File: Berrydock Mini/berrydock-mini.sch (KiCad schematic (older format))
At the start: 96 parts, among them J1 RJ45, P1 CONN_01X18, P2 CONN_01X18, P3 CONN_01X04, P4 CONN_01X02, P5 USB_OTG, P6 USB_A, SW1 SWITCH_INV, SW2 BUTTON, U1 USBLC6-2, U10 L6920DC, U11 FS8205A, U12 DW01-P, U13 USBLC6-2, U14 ADS1015, U15 USBLC6-2, U16 CP2102, U2 USBLC6-2, U3 AMS1117, U4 H1260NL, U5 Omega2, U6 SMP75, U7 SMP75, U8 ACT4088, U9 MCP73831

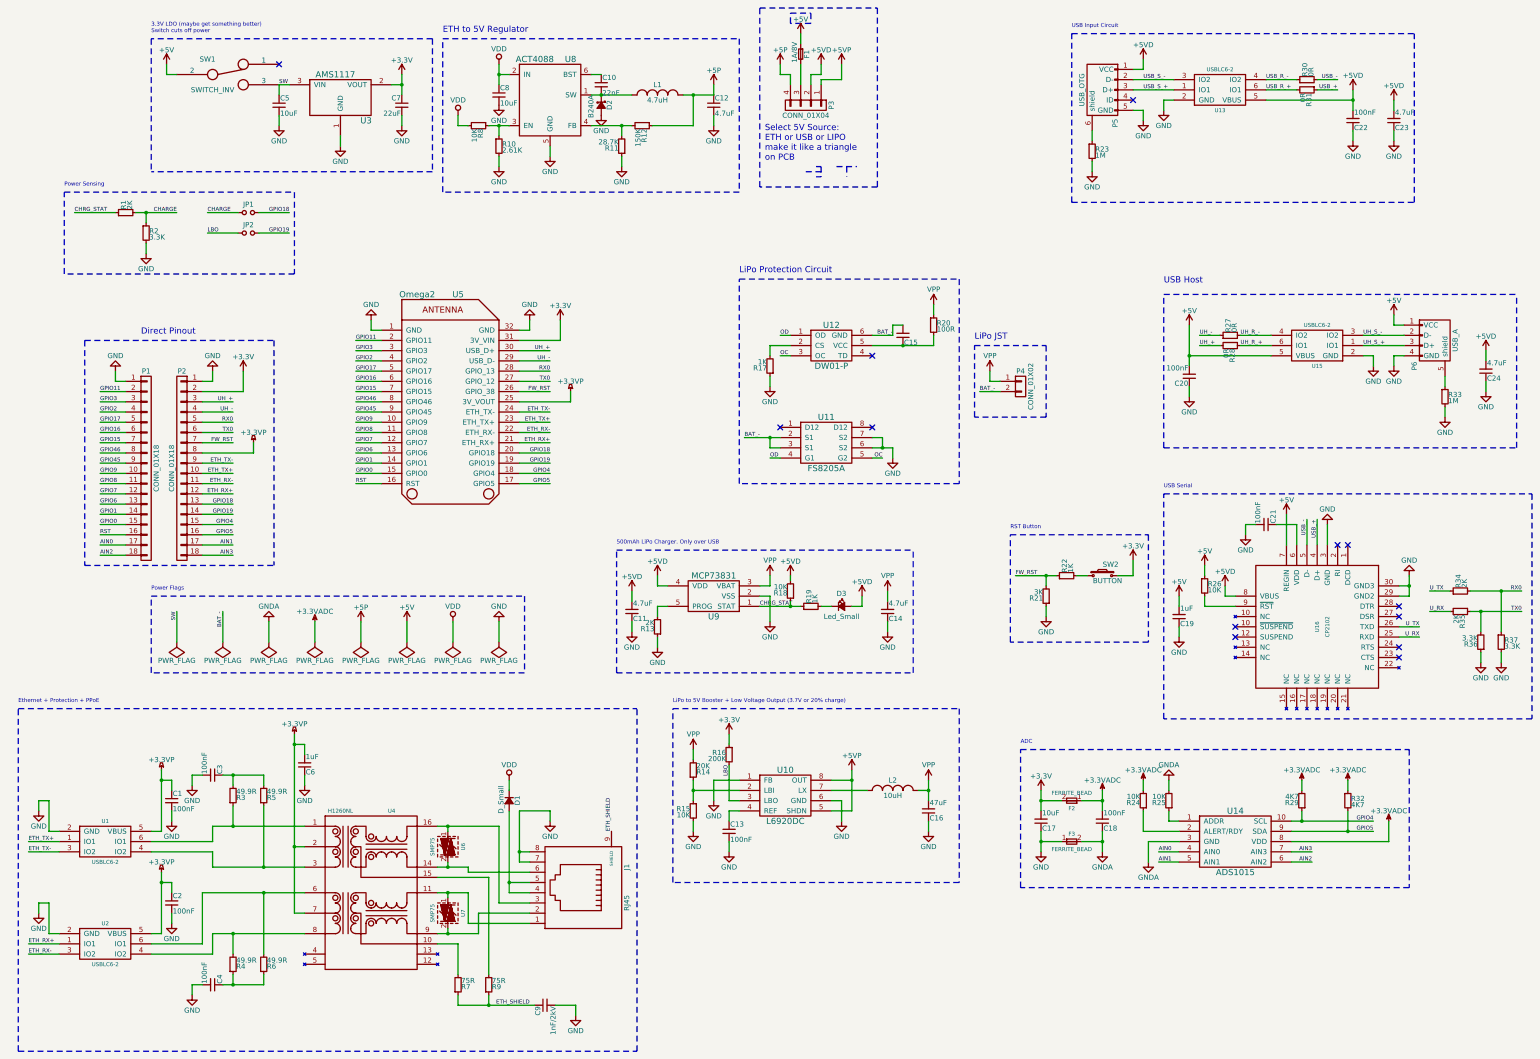
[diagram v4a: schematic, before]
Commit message: Added many footprint
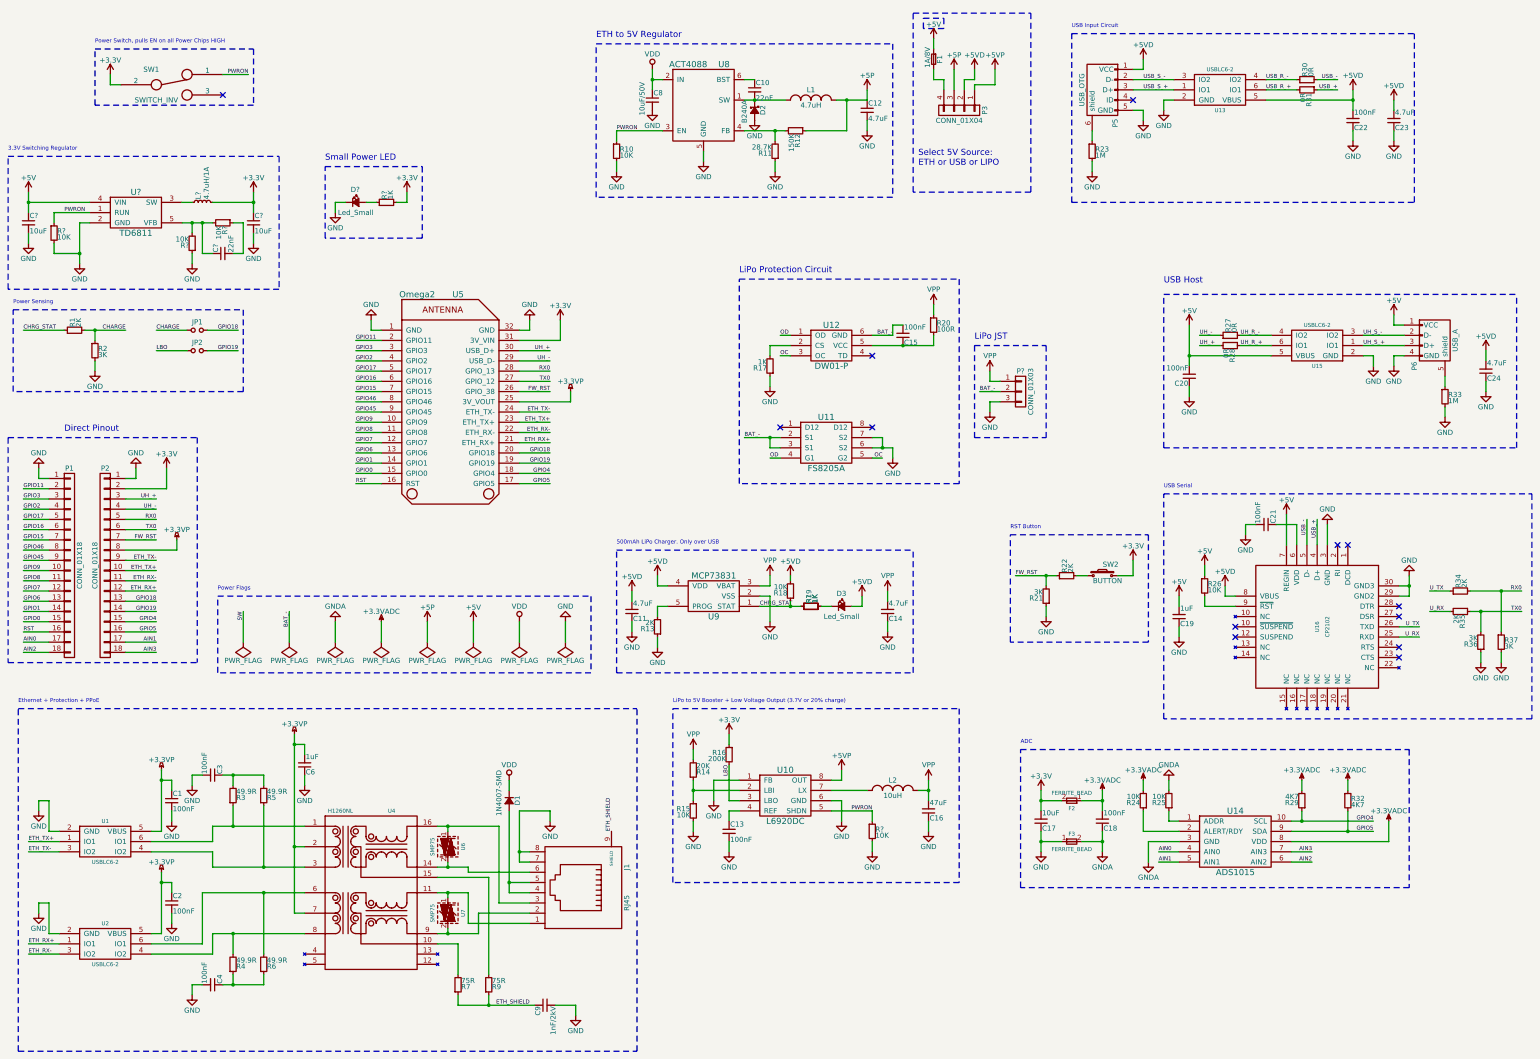
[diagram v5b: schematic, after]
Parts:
- removed C5: 10uF, Capacitors_SMD:C_0603, symbol C_Small
- removed C7: 22uF, Capacitors_SMD:C_0603, symbol C_Small
- removed P4: CONN_01X02, symbol CONN_01X02
- removed R8: 10K, Resistors_SMD:R_0603_HandSoldering, symbol R_Small
- removed U3: AMS1117, symbol AMS1117
- added C? (x2): 10uF, Capacitors_SMD:C_1206, symbol C_Small
- added C?: 22nF, Capacitors_SMD:C_1206, symbol C_Small
- added D?: Led_Small, LEDs:LED_0805, symbol Led_Small
- added L?: 4.7uH/1A, symbol L_Small
- added P?: CONN_01X03, Omega2-Berrydock:JST-RIGHT-ANGLE, symbol CONN_01X03
- added R? (x2): 1K, Resistors_SMD:R_0603_HandSoldering, symbol R_Small
- added R? (x4): 10K, Resistors_SMD:R_0603_HandSoldering, symbol R_Small
- added U?: TD6811, symbol TD6811
- C1, C11: footprint (none) -> Capacitors_SMD:C_0603
- C15: value Capacitors_SMD:C_0603 -> 100nF; footprint (none) -> Capacitors_SMD:C_0603
- C8: value 10uF -> 10uF/50V
- D1: value D_Small -> 1N4007-SMD; footprint (none) -> Omega2-Berrydock:DO-214AC.SMA
- D2: footprint (none) -> Omega2-Berrydock:DO-214AC.SMA
- D3: footprint (none) -> LEDs:LED_0805
- J1: footprint (none) -> Omega2-Berrydock:RJ45-SHIELDED
- JP1, JP2: footprint (none) -> Pin_Headers:Pin_Header_Straight_1x02
- L1: footprint (none) -> Omega2-Berrydock:CD32
- P3: footprint (none) -> Omega2-Berrydock:PWR-SELECT
- P5: footprint (none) -> Connect:USB_Micro-B
- P6: footprint (none) -> Connect:USB_A
- R10: value 2.61K -> 10K
- R2, R36, R37: value 3.3K -> 3K
- R22: value 1K -> 2K
- U1, U13, U15, U2: footprint (none) -> Omega2-Berrydock:SOT32-6L
- U11: footprint (none) -> Omega2-Berrydock:TSSOP8
- U12, U8: footprint (none) -> TO_SOT_Packages_SMD:SOT-23-6_Handsoldering
- U16: footprint (none) -> Housings_DFN_QFN:QFN-28-1EP_5x5mm_Pitch0.5mm
- U4: footprint (none) -> Omega2-Berrydock:HL1260NL
- U5: footprint (none) -> Omega2-Berrydock:Omega2-Outline
- U6, U7: footprint (none) -> Omega2-Berrydock:DO-214AA
- U9: footprint (none) -> TO_SOT_Packages_SMD:SOT-23-5
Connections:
- net +3V3: now also SW1.2, C?.1, L?.2, R?.2
- net +5P: now also P3.3 (P3); no longer P3.4 (P4)
- net +5V: now also C?.1, U?.4 (VIN); no longer SW1.2
- net +5VP: no longer U10.5 (SHDN)
- net BAT_-: now also P?.2 (P2)
- net CHRG_STAT: now also R?.1
- net GND: now also C?.2, C?.2, D?.1 (K), P?.3 (P3), R?.1, R?.2, R?.2, U?.2 (GND)
- net SW: no longer SW1.3
- net VPP: now also P?.1 (P1)
- net PWRON: now reaches R10.1, U8.3 (EN)
- net PWRON: now also SW1.1, U10.5 (SHDN), R?.1, R?.1, U?.1 (RUN)
- net at F1.2: now also P3.4 (P4); no longer P3.3 (P3)
- net at D3.1 (K), R19.2: now also R?.2
- new net: L?.1, U?.3 (SW)
- new net: C?.1, R?.2, R?.2, U?.5 (VFB)
- new net: C?.2, R?.1
- new net: D?.2 (A), R?.1
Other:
- note added: "3.3V Switching Regulator"
- note added: "Power Switch, pulls EN on all Power Chips HIGH"
- note added: "Select 5V Source:\nETH or USB or LIPO\n"
- note added: "Small Power LED"
- note removed: "3.3V LDO (maybe get something better)\nSwitch cuts off power"
- note removed: "Select 5V Source:\nETH or USB or LIPO\nmake it like a triangle\non PCB"
- moved on the sheet: C10, C12, C8, D2, F1, JP1, JP2, L1, P1, P2, P3, R1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

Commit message: fixed errors, new naming of items
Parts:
- gave numbers to parts that had none: 13
- renumbered C8 to C10, C13 to C12, C10 to C13, C12 to C14, C14 to C17, C17 to C18, C18 to C19, C1 to C2, C19 to C20, C20 to C21, C21 to C22, C22 to C23, C23 to C24, C24 to C25, C2 to C3, C3 to C4, C4 to C5, C6 to C8, D1 to D2, D2 to D3, D3 to D4, L1 to L2, L2 to L3, R7 to R11, R9 to R12, R10 to R13, R13 to R16, R16 to R17, R17 to R18, R11 to R19, R1 to R2, R12 to R20, R18 to R21, R19 to R22, R20 to R25, R21 to R26, R22 to R27, R23 to R28, R24 to R29, R2 to R3, R25 to R30, R26 to R31, R27 to R32, R28 to R33, R29 to R34, R30 to R35, R31 to R36, R32 to R37, R33 to R38, R34 to R39, R35 to R40, R36 to R41, R37 to R42, R3 to R6, R4 to R7, R5 to R8, R6 to R9
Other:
- moved on the sheet: C11, C17, D4, R16, R21, R22, R23, U9

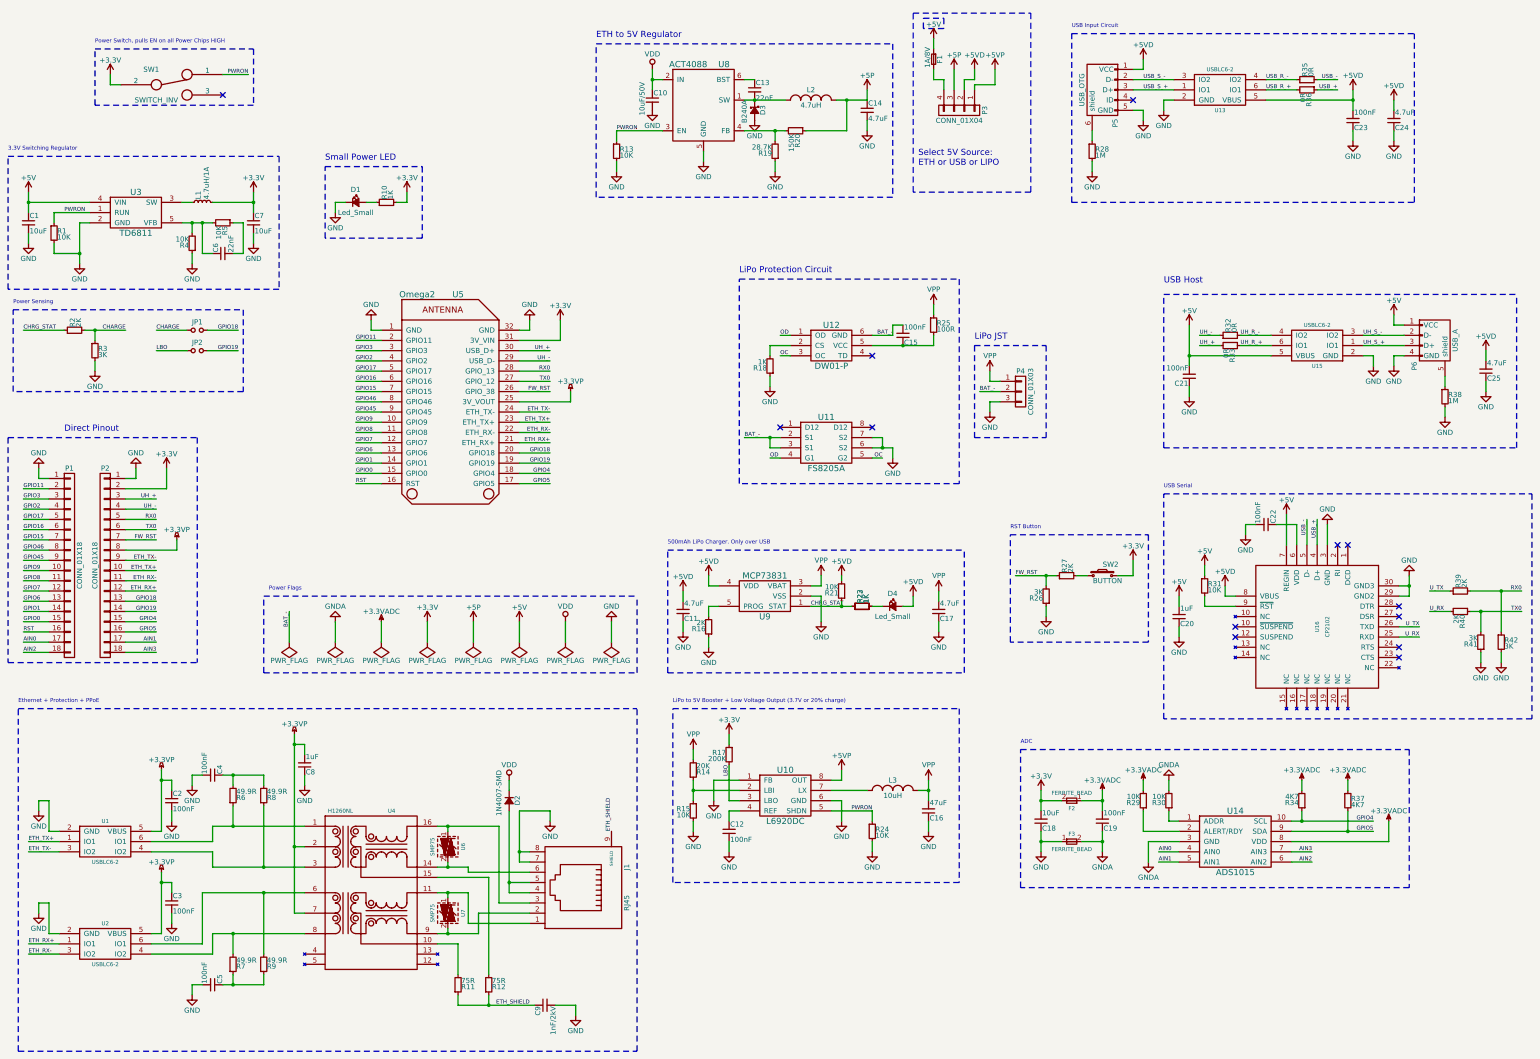
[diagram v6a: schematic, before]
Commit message: Added all footprints
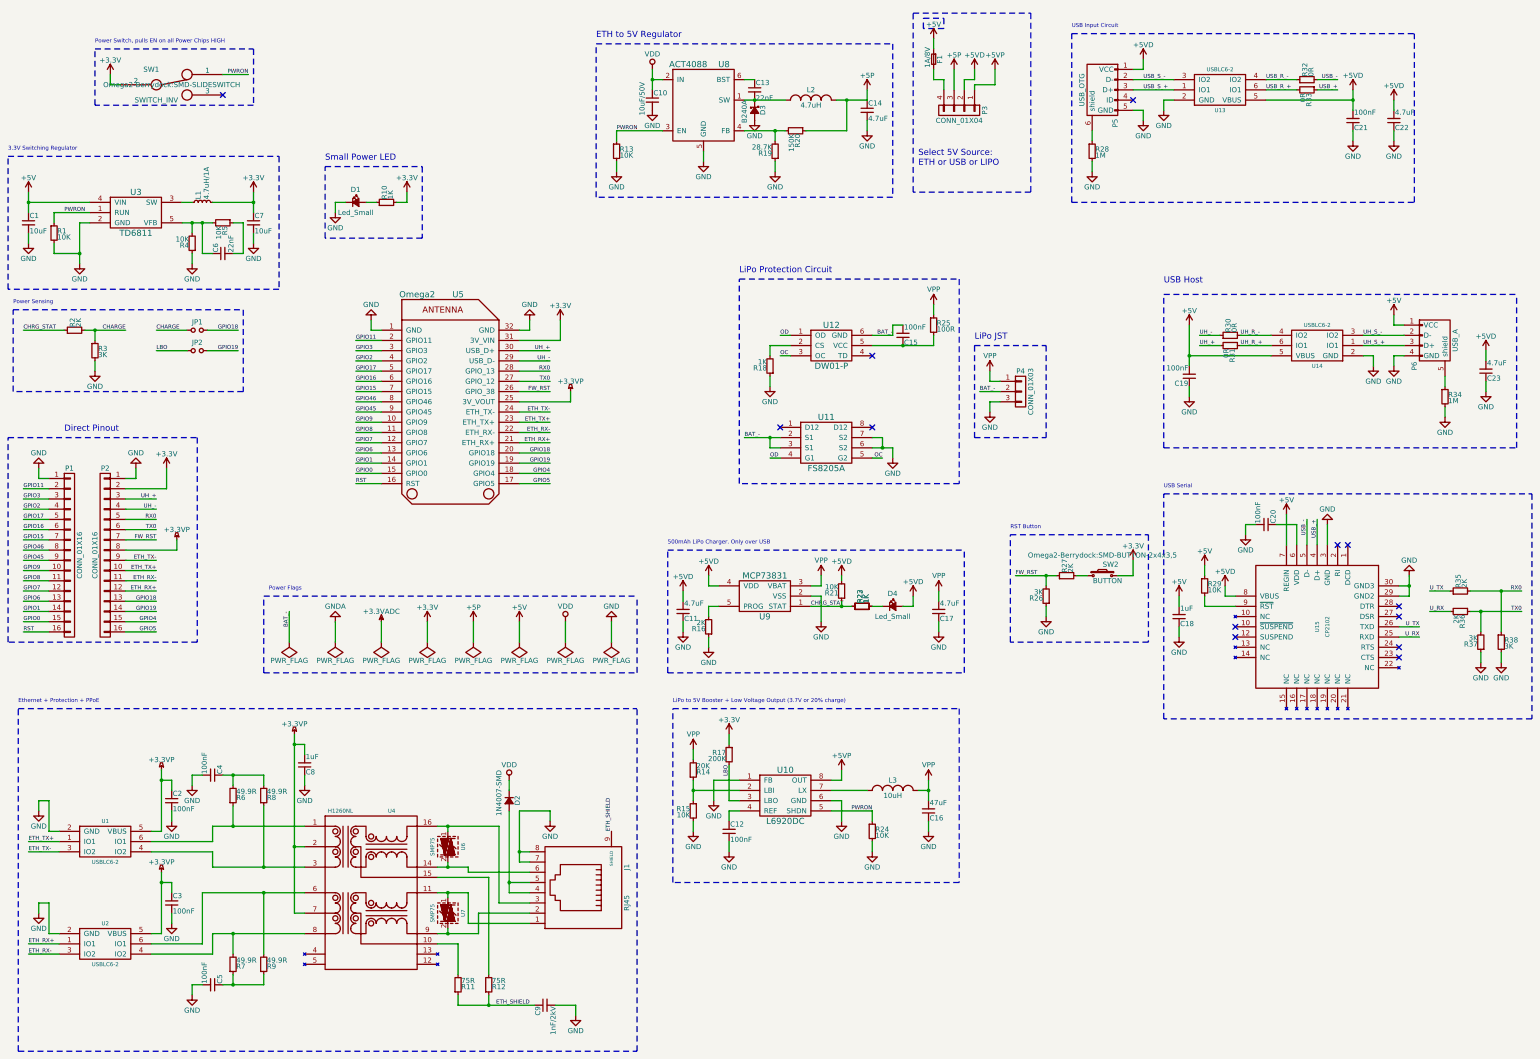
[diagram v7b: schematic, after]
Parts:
- removed C18: 10uF, Capacitors_SMD:C_0603, symbol C_Small
- removed C19: 100nF, Capacitors_SMD:C_0603, symbol C_Small
- removed F2, F3: FERRITE_BEAD, symbol FERRITE_BEAD
- removed P1, P2: CONN_01X18, Pin_Headers:Pin_Header_Straight_1x18, symbol CONN_01X18
- removed R29, R30: 10K, Resistors_SMD:R_0603_HandSoldering, symbol R_Small
- removed R34, R37: 4K7, Resistors_SMD:R_0603_HandSoldering, symbol R_Small
- removed U14: ADS1015, symbol ADS1015
- added P1, P2: CONN_01X16, Pin_Headers:Pin_Header_Straight_1x16, symbol CONN_01X16
- C19: renamed from C21; footprint (none) -> Capacitors_SMD:C_0603
- C8: footprint (none) -> Capacitors_SMD:C_0603
- F1: footprint (none) -> Omega2-Berrydock:FUSE-1812
- L1: footprint (none) -> Omega2-Berrydock:CD32
- L3: footprint (none) -> Omega2-Berrydock:CD43
- SW1: footprint (none) -> Omega2-Berrydock:SMD-SLIDESWITCH
- SW2: footprint (none) -> Omega2-Berrydock:SMD-BUTTON-2x4x3,5
- U10: footprint (none) -> Omega2-Berrydock:MSOP8
- U3: footprint (none) -> TO_SOT_Packages_SMD:SOT-23-5
- renumbered C20 to C18, C22 to C20, C23 to C21, C24 to C22, C25 to C23, R31 to R29, R32 to R30, R33 to R31, R35 to R32, R36 to R33, R38 to R34, R39 to R35, R40 to R36, R41 to R37, R42 to R38, U15 to U14, U16 to U15
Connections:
- net +3.3VP: now also P2.8 (P8)
- net +3V3: now also P2.2 (P2)
- net ETH_RX+: now also P2.12 (P12)
- net ETH_RX-: now also P2.11 (P11)
- net ETH_TX+: now also P2.10 (P10)
- net ETH_TX-: now also P2.9 (P9)
- net FW_RST: now also P2.7 (P7)
- net GND: now also P1.1 (P1), P2.1 (P1)
- net GPIO0: now also P1.15 (P15)
- net GPIO1: now also P1.14 (P14)
- net GPIO11: now also P1.2 (P2)
- net GPIO15: now also P1.7 (P7)
- net GPIO16: now also P1.6 (P6)
- net GPIO17: now also P1.5 (P5)
- net GPIO18: now also P2.13 (P13)
- net GPIO19: now also P2.14 (P14)
- net GPIO2: now also P1.4 (P4)
- net GPIO3: now also P1.3 (P3)
- net GPIO4: now also P2.15 (P15)
- net GPIO45: now also P1.9 (P9)
- net GPIO46: now also P1.8 (P8)
- net GPIO5: now also P2.16 (P16)
- net GPIO6: now also P1.13 (P13)
- net GPIO7: now also P1.12 (P12)
- net GPIO8: now also P1.11 (P11)
- net GPIO9: now also P1.10 (P10)
- net RST: now also P1.16 (P16)
- net RX0: now also P2.5 (P5)
- net TX0: now also P2.6 (P6)
- net UH_+: now also P2.3 (P3)
- net UH_-: now also P2.4 (P4)
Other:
- note removed: "ADC"
